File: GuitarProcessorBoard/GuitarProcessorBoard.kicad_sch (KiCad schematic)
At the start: 0 parts

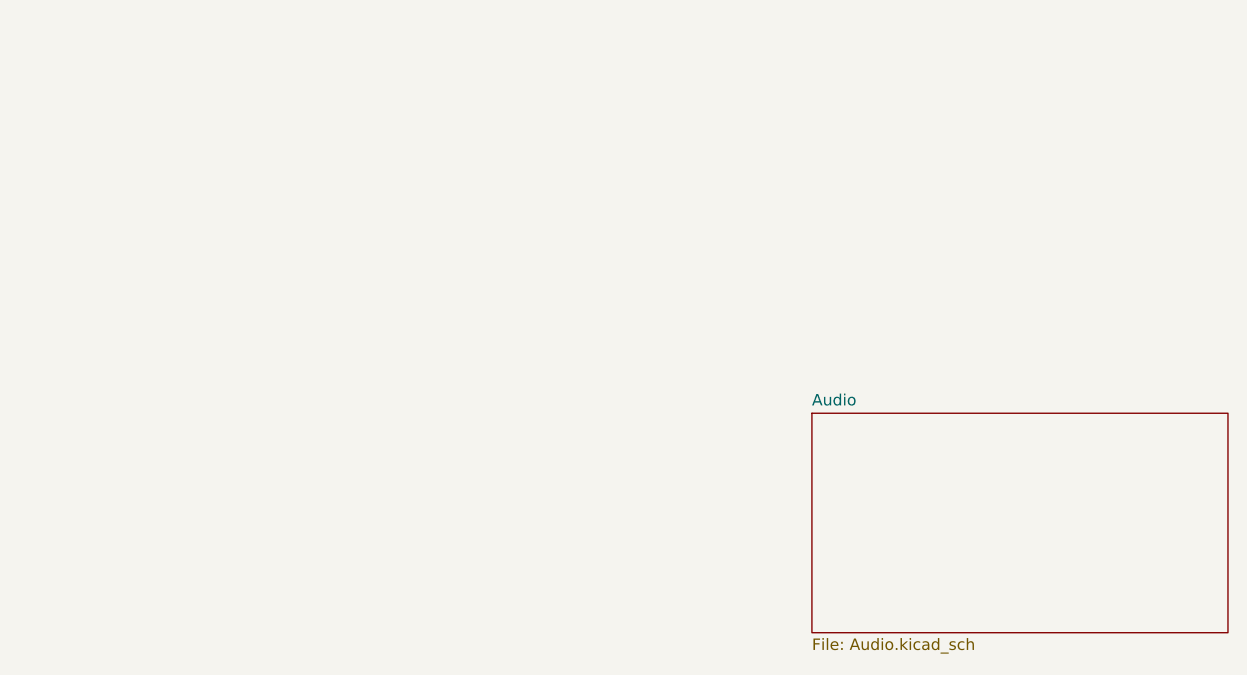
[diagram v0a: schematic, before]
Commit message: basic MCU pinout, IO headers
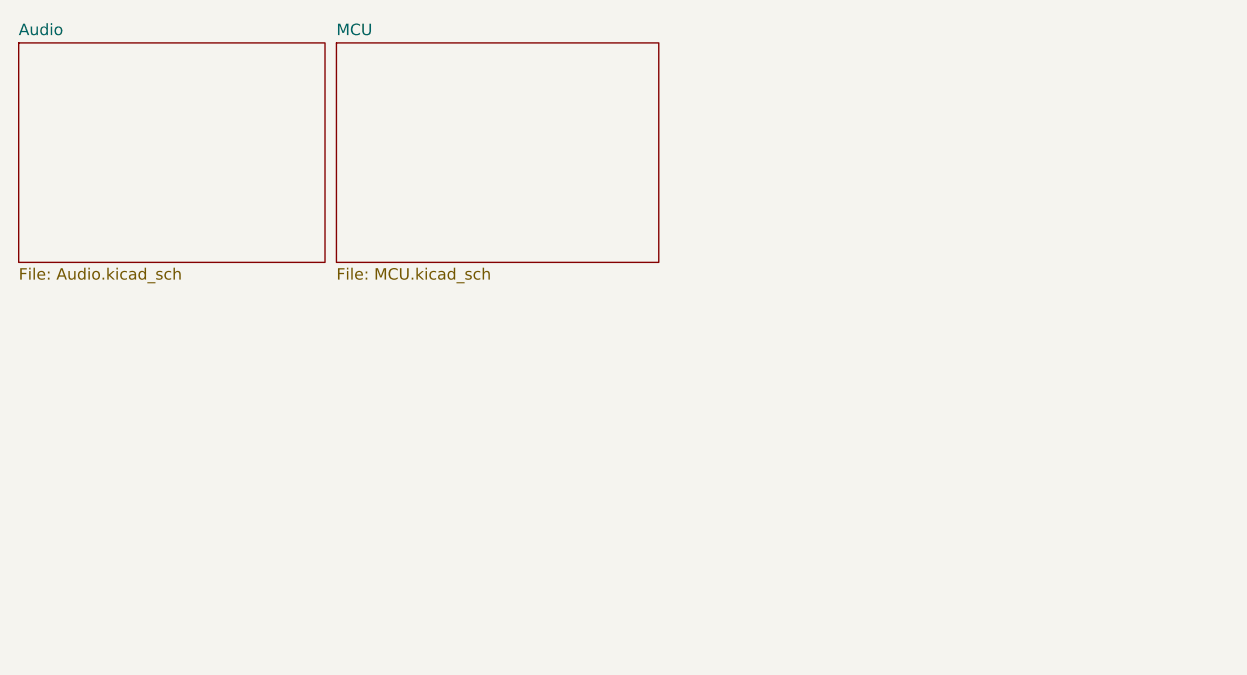
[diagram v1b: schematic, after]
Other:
- added sheet MCU (MCU.kicad_sch)
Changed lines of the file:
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@@
 	(paper "A4")
 	(sheet
-		(at 108.458 68.326)
-		(size 46.228 24.384)
+		(at 55.626 27.178)
+		(size 35.814 24.384)
+		(fields_autoplaced yes)
+		(stroke
+			(width 0.1524)
+			(type solid)
+		)
+		(fill
+			(color 0 0 0 0.0000)
+		)
+		(property "Sheetname" "MCU"
+			(at 55.626 26.4664 0)
+			(effects
+				(font
+					(size 1.27 1.27)
+				)
+				(justify left bottom)
+			)
+		)
+		(property "Sheetfile" "MCU.kicad_sch"
+			(at 55.626 52.1466 0)
+			(effects
+				(font
+					(size 1.27 1.27)
+				)
+				(justify left top)
+			)
+		)
+		(instances
+			(project "GuitarProcessorBoard"
+				(path "/524c695b-c632-4089-9e9a-ef0f89cad1b2"
+					(page "3")
+				)
+			)
+		)
+	)
+	(sheet
+		(at 20.32 27.178)
+		(size 34.036 24.384)
 		(fields_autoplaced yes)
 		(stroke
@@
 		)
 		(property "Sheetname" "Audio"
-			(at 108.458 67.6144 0)
+			(at 20.32 26.4664 0)
 			(effects
 				(font
@@
 		)
 		(property "Sheetfile" "Audio.kicad_sch"
-			(at 108.458 93.2946 0)
+			(at 20.32 52.1466 0)
 			(effects
 				(font
